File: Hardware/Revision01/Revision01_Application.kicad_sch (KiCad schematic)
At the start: 32 parts, among them J1 Conn_02x08_Odd_Even, J3 Conn_02x08_Odd_Even, J4 Conn_01x04, Q2 PMV32UP,215, Q3 PMV32UP,215, U2 AD7124-8BCPZ-RL7, U3 MRF89XAM9AT-I/RM, U4 ICM-45605

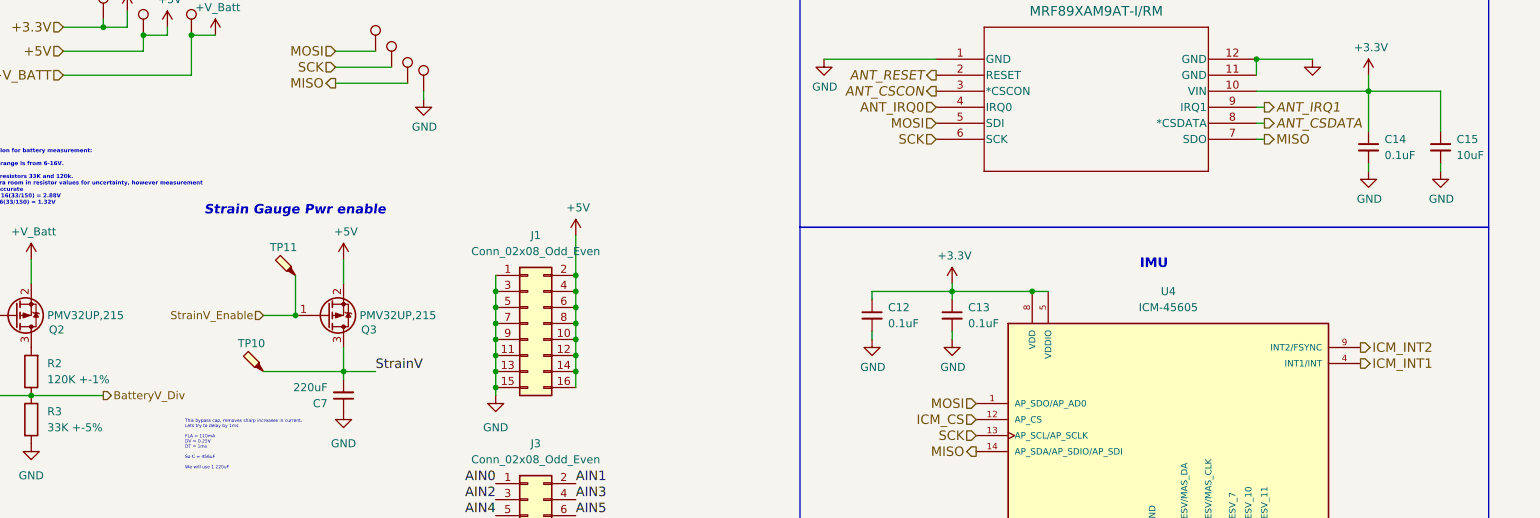
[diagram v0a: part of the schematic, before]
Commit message: started wiring modules together
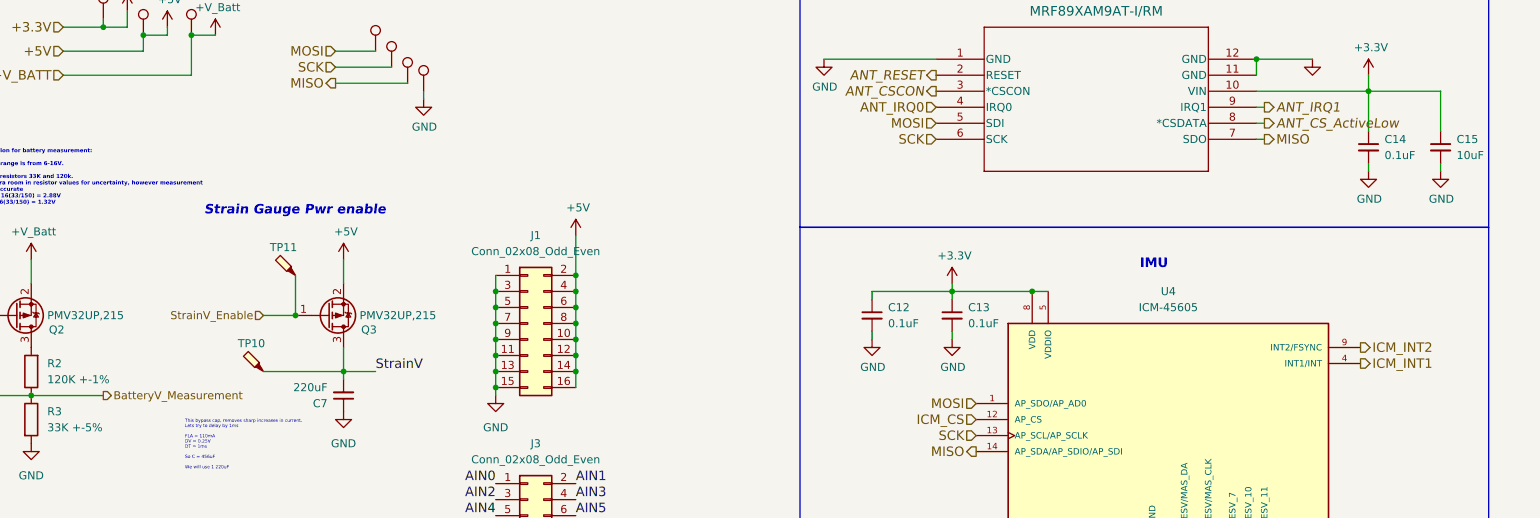
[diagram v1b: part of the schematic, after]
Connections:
- net ANT_CSDATA renamed ANT_CS_ActiveLow
- net BatteryV_Div renamed BatteryV_Measurement
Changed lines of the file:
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@@
 		)
 	)
-	(hierarchical_label "ANT_CSDATA"
+	(hierarchical_label "ANT_CS_ActiveLow"
 		(shape output)
 		(at 246.38 39.37 0)
@@
 		)
 	)
-	(hierarchical_label "BatteryV_Div"
+	(hierarchical_label "BatteryV_Measurement"
 		(shape output)
 		(at 62.23 82.55 0)

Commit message: neated up the circuit - done wire-accross sheets - done Ensure all components have footprints - done Create net classes - DONE 	POWER 	GND 	SPI 	GPIO
Add in new components into BOM
	- Power switch, exclude from BOM - DONE - added component to switch. Not sure how to get it to work
	- Add in the resistors in parallel and series. for SPI busses - Done(PENDING whether to take series resistors out)
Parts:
- removed TP12, TP13, TP14, TP15, TP5, TP6, TP7: TestPoint, TestPoint:TestPoint_THTPad_1.0x1.0mm_Drill0.5mm, symbol Connector:TestPoint
- C15: footprint Capacitor_SMD:C_1206_3216Metric -> CAP_1812Z_AVX; Distributor link (none) -> https://www.digikey.ca/en/products/detail/kyocera-avx/18123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; Manufacturer (none) -> KYOCERA AVX; Manufacturer Part Number (none) -> 18123D106KAT2A
- C7: Distributor Link https://www.digikey.ca/en/products/detail/taiyo-yuden/JMK32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 -> (none); Distributor link (none) -> https://www.digikey.ca/en/products/detail/taiyo-yuden/JMK32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; Manufacturer Part Number (none) -> JMK325ABJ227MM-T
- R2: Distributor Link https://www.digikey.ca/en/products/detail/koa-speer-electro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 -> (none); Distributor link (none) -> https://www.digikey.ca/en/products/detail/koa-speer-electro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; Manufacturer Part Number (none) -> RK73H2ATTD1203F
- R3: Distributor link (none) -> https://www.digikey.ca/en/products/detail/stackpole-electro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; Manufacturer (none) -> Stackpole Electronics Inc; Manufacturer Part Number (none) -> RMCF0805JT33K0
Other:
- note added: "ADC"
- note removed: "10K https://www.digikey.com/en/products/detail/stackpole-electronics-inc/RMCF0805JT10K0/1757762 50 ohms https://www.digikey.com/en/products/detail/stackpole-electronics-inc/RMCF0805JT10R0/1757791"
- note removed: "LED - link https://www.digikey.ca/en/products/detail/carling-technologies/LRA211-RS-B-125N/3025014?gclsrc=aw.ds&&utm_adgroup=General&utm_source=google&utm_medium=cpc&utm_campaign=PMax%20Shopping_Product_Zombie%20SKUs&utm_term=&productid=3025014&utm_content=General&utm_id=go_cmp-17855401585_adg-_ad-__dev-c_ext-_prd-3025014_sig-CjwKCAjwnPS-BhBxEiwAZjMF0mF0fCE8VqqB3_4b_FOh5KWq0rT26TiGIuxADLE69xiFPgr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"
- note removed: "Mainly verified and fixed peripheral component selection MOSFET-WIREOUT - DONE ANTENNA WIRE-OUT - DONE ADC WIRE-OUT - DONE - found error in ADC wireout, EP was left unconnected - notes on pins I found a bit confusing has been addressed, and notes are left around component IMU WIRE-OUT - DONE CHECK COMPONENT SELECTION ON MOSFET - Done Need to pick 100K component and 33K components - Done ADC - Don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"
- note removed: "Reference design is unclear. Please go review extra carefully on ADC https://www.analog.com/en/products/ad7124-8.html#reference-designs"
- note removed: "TO DO SHEET ADD TEST POINTS FOR POWER RAILS AND COMM PORTS - finished ADD POWER SWITCH WITH INTEGRATED LED <--- finished ADD SERIES AND PULL-UP RESISTORS TO SPI-BUS <--- finished"
- moved on the sheet: C10, C11, C3, C6, C7, C8, C9, J1, J3, J4, Q2, Q3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

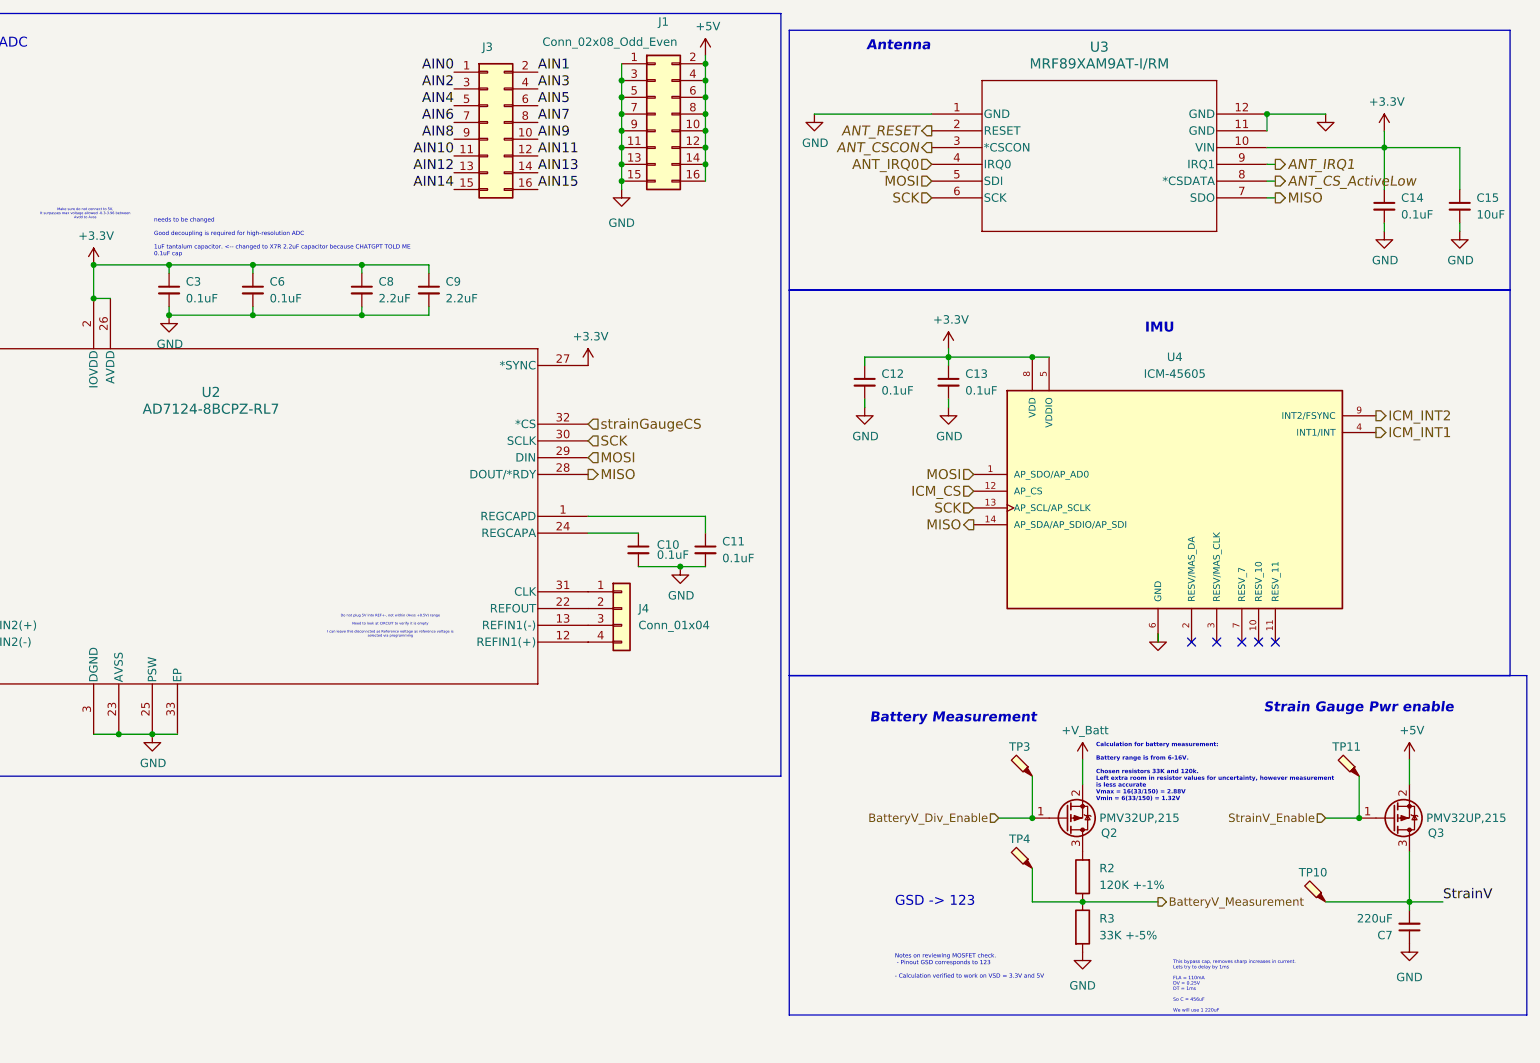
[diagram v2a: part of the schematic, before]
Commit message: CREATE STM32CUBEIDE file to verify all ports Check over CONTROLLER SHEET Improve annotation ordering Move testpoints out of controller sheet
Still performering ERC check
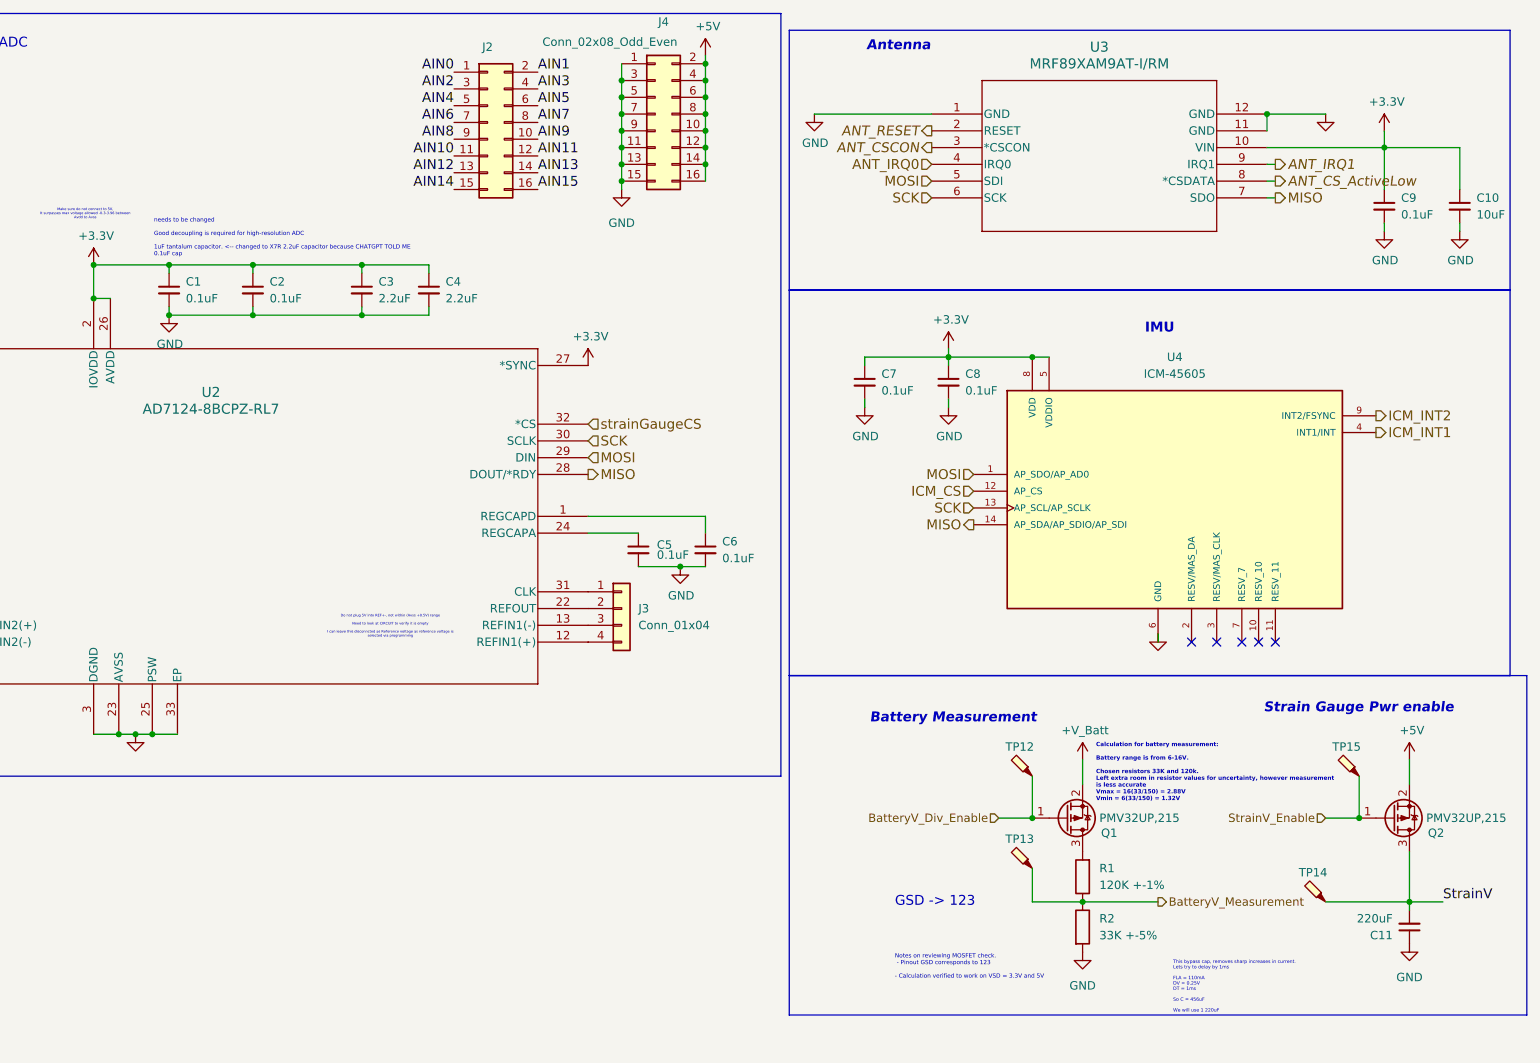
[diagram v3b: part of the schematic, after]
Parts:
- renumbered C3 to C1, C15 to C10, C7 to C11, C6 to C2, C8 to C3, C9 to C4, C10 to C5, C11 to C6, C12 to C7, C13 to C8, C14 to C9, J3 to J2, J4 to J3, J1 to J4, Q2 to Q1, Q3 to Q2, R2 to R1, R3 to R2, TP3 to TP12, TP4 to TP13, TP10 to TP14, TP11 to TP15

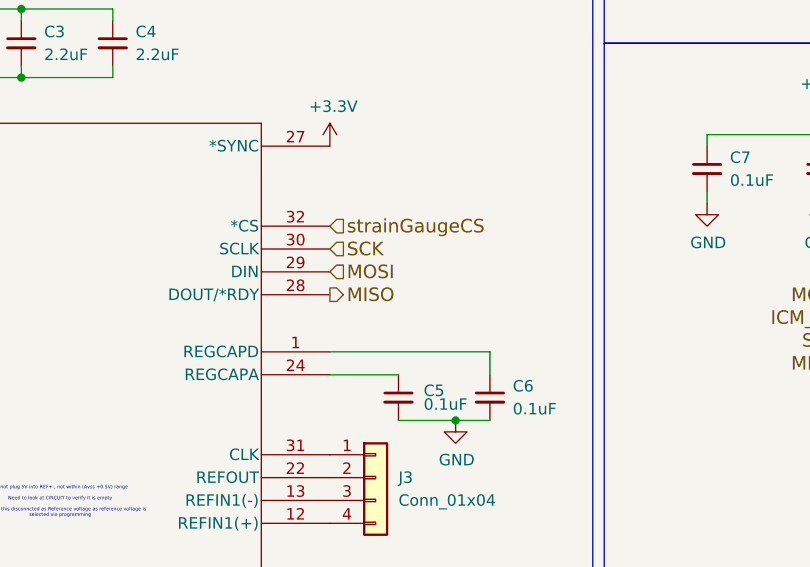
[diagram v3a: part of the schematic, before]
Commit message: made some progress on ERC
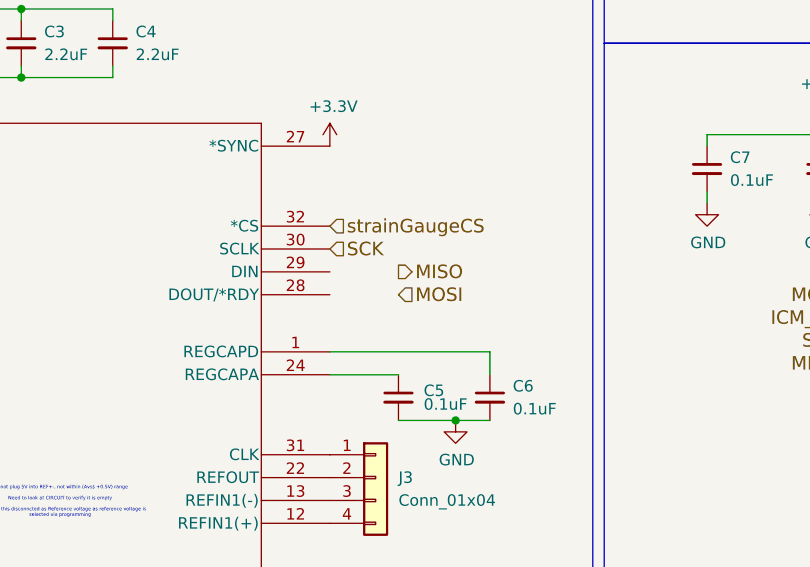
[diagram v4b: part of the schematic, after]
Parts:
- C10: footprint CAP_1812Z_AVX -> Capacitor_SMD:C_0805_2012Metric
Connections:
- net MISO: no longer U2.28 (DOUT/*RDY)
- net MOSI: no longer U2.29 (DIN)
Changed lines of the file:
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@@
 	(hierarchical_label "MISO"
 		(shape output)
-		(at 142.24 83.82 0)
+		(at 149.86 81.28 0)
 		(effects
 			(font
@@
 	(hierarchical_label "MOSI"
 		(shape input)
-		(at 142.24 81.28 0)
+		(at 149.86 83.82 0)
 		(effects
 			(font
@@
 			)
 		)
-		(property "Footprint" "CAP_1812Z_AVX"
+		(property "Footprint" "Capacitor_SMD:C_0805_2012Metric"
 			(at 274.32 43.18 0)
 			(effects
